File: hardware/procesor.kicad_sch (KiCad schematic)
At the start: 14 parts

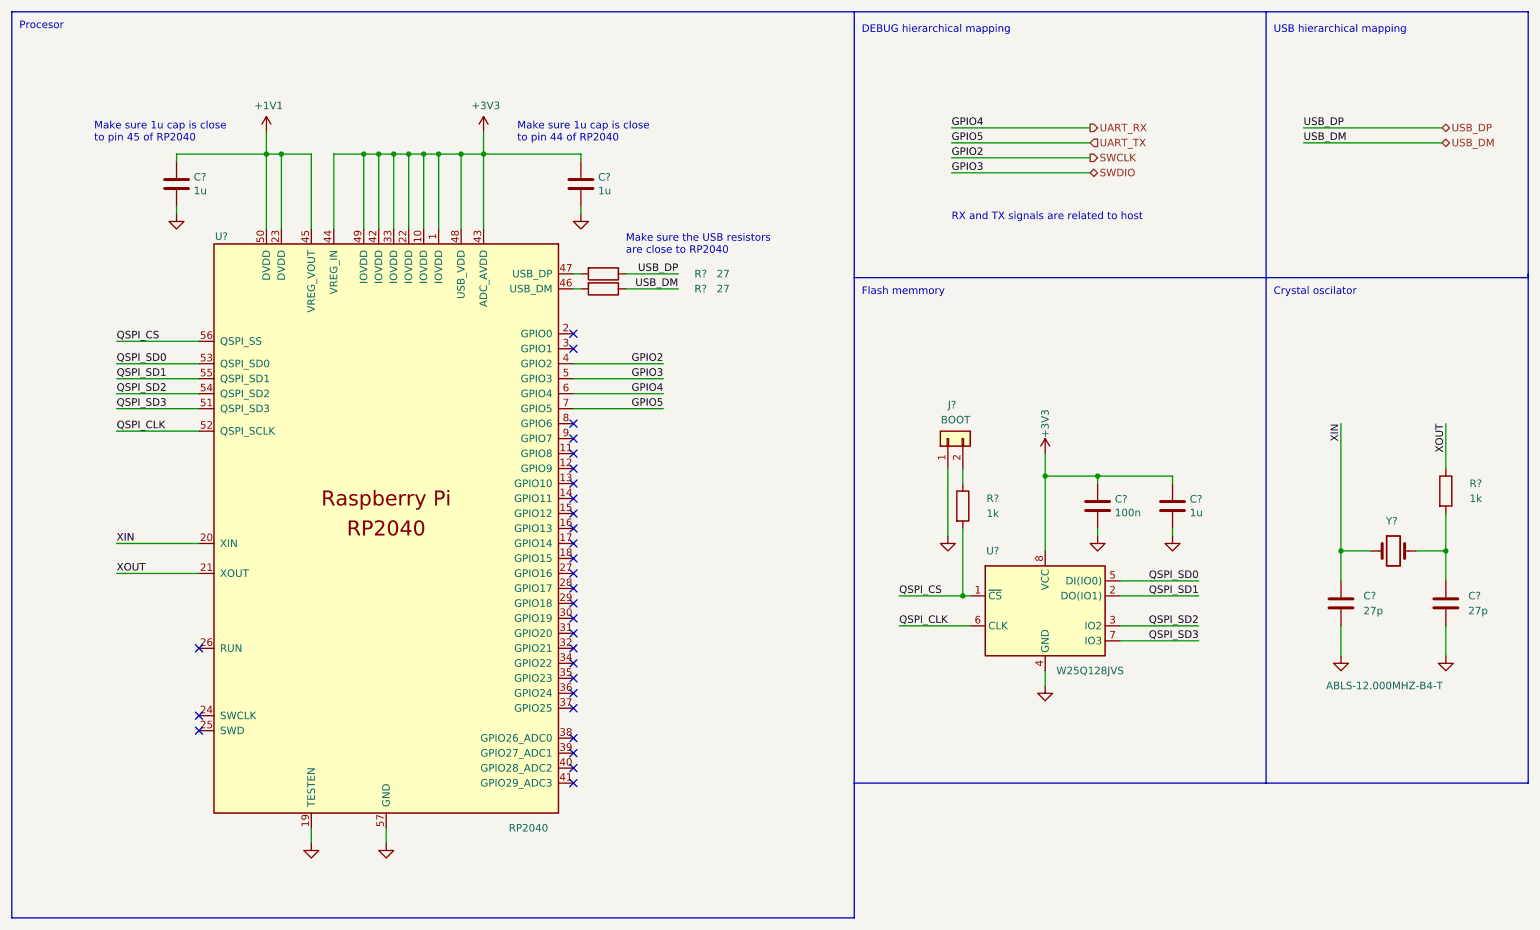
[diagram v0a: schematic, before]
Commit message: hw: Add annotations to all components
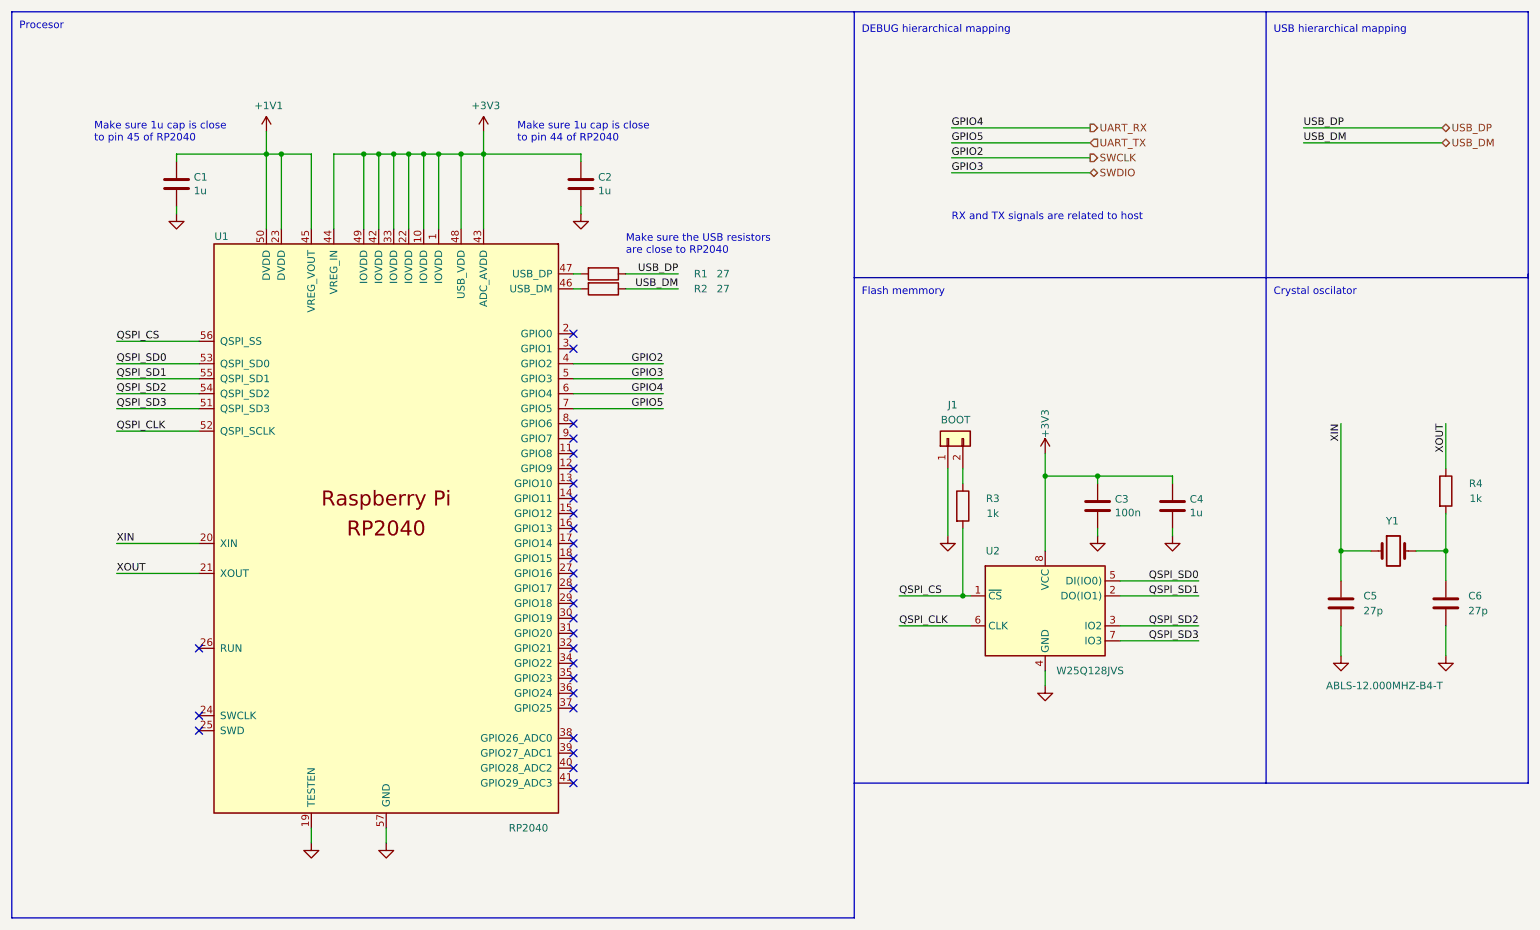
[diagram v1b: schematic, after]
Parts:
- gave numbers to parts that had none: 14
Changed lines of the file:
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@@
   (no_connect (at 114.935 158.115))
   (no_connect (at 114.935 160.655))
+  (no_connect (at 51.435 137.795))
   (no_connect (at 51.435 151.765))
   (no_connect (at 51.435 149.225))
-  (no_connect (at 51.435 137.795))
   (wire (pts (xy 99.695 50.165) (xy 99.695 53.975))
     (stroke (width 0) (type default) (color 0 0 0 0))
@@
   (symbol (lib_id "power:GND") (at 216.535 118.745 0) (unit 1)
     (in_bom yes) (on_board yes)
-    (property "Reference" "#PWR?" (id 0) (at 216.535 125.095 0)
+    (property "Reference" "#PWR011" (id 0) (at 216.535 125.095 0)
       (effects (font (size 1.27 1.27)) hide)
     )
@@
   (symbol (lib_id "Device:C") (at 116.205 59.055 0) (unit 1)
     (in_bom yes) (on_board yes)
-    (property "Reference" "C?" (id 0) (at 119.126 57.8866 0)
+    (property "Reference" "C2" (id 0) (at 119.126 57.8866 0)
       (effects (font (size 1.27 1.27)) (justify left))
     )
@@
   (symbol (lib_id "Device:C") (at 216.535 113.665 0) (unit 1)
     (in_bom yes) (on_board yes)
-    (property "Reference" "C?" (id 0) (at 219.456 112.4966 0)
+    (property "Reference" "C4" (id 0) (at 219.456 112.4966 0)
       (effects (font (size 1.27 1.27)) (justify left))
     )
@@
   (symbol (lib_id "power:GND") (at 83.185 170.815 0) (unit 1)
     (in_bom yes) (on_board yes)
-    (property "Reference" "#PWR?" (id 0) (at 83.185 177.165 0)
+    (property "Reference" "#PWR04" (id 0) (at 83.185 177.165 0)
       (effects (font (size 1.27 1.27)) hide)
     )
@@
   (symbol (lib_id "Device:R") (at 262.89 111.125 0) (unit 1)
     (in_bom yes) (on_board yes)
-    (property "Reference" "R?" (id 0) (at 267.97 109.855 0))
+    (property "Reference" "R4" (id 0) (at 267.97 109.855 0))
     (property "Value" "1k" (id 1) (at 267.97 112.395 0))
     (property "Footprint" "Capacitor_SMD:C_0603_1608Metric_Pad1.08x0.95mm_HandSolder" (id 2) (at 261.112 111.125 90)
@@
   (symbol (lib_id "Device:C") (at 47.625 59.055 0) (unit 1)
     (in_bom yes) (on_board yes)
-    (property "Reference" "C?" (id 0) (at 50.546 57.8866 0)
+    (property "Reference" "C1" (id 0) (at 50.546 57.8866 0)
       (effects (font (size 1.27 1.27)) (justify left))
     )
@@
   (symbol (lib_id "Memory_Flash:W25Q128JVS") (at 194.945 131.445 0) (unit 1)
     (in_bom yes) (on_board yes)
-    (property "Reference" "U?" (id 0) (at 186.055 121.285 0))
+    (property "Reference" "U2" (id 0) (at 186.055 121.285 0))
     (property "Value" "W25Q128JVS" (id 1) (at 202.565 141.605 0))
     (property "Footprint" "Package_SO:SOIC-8_5.23x5.23mm_P1.27mm" (id 2) (at 194.945 131.445 0)
@@
   (symbol (lib_id "power:GND") (at 47.625 64.135 0) (unit 1)
     (in_bom yes) (on_board yes)
-    (property "Reference" "#PWR?" (id 0) (at 47.625 70.485 0)
+    (property "Reference" "#PWR01" (id 0) (at 47.625 70.485 0)
       (effects (font (size 1.27 1.27)) hide)
     )
@@
   (symbol (lib_id "Device:C") (at 245.11 130.175 0) (unit 1)
     (in_bom yes) (on_board yes)
-    (property "Reference" "C?" (id 0) (at 248.92 128.905 0)
+    (property "Reference" "C5" (id 0) (at 248.92 128.905 0)
       (effects (font (size 1.27 1.27)) (justify left))
     )
@@
   (symbol (lib_id "Device:C") (at 203.835 113.665 0) (unit 1)
     (in_bom yes) (on_board yes)
-    (property "Reference" "C?" (id 0) (at 206.756 112.4966 0)
+    (property "Reference" "C3" (id 0) (at 206.756 112.4966 0)
       (effects (font (size 1.27 1.27)) (justify left))
     )
@@
   (symbol (lib_id "power:GND") (at 178.435 118.745 0) (unit 1)
     (in_bom yes) (on_board yes)
-    (property "Reference" "#PWR?" (id 0) (at 178.435 125.095 0)
+    (property "Reference" "#PWR07" (id 0) (at 178.435 125.095 0)
       (effects (font (size 1.27 1.27)) hide)
     )
@@
   (symbol (lib_id "Device:Crystal") (at 254 121.285 0) (unit 1)
     (in_bom yes) (on_board yes)
-    (property "Reference" "Y?" (id 0) (at 252.73 116.205 0)
+    (property "Reference" "Y1" (id 0) (at 252.73 116.205 0)
       (effects (font (size 1.27 1.27)) (justify left))
     )
@@
   (symbol (lib_id "power:+1V1") (at 62.865 50.165 0) (unit 1)
     (in_bom yes) (on_board yes)
-    (property "Reference" "#PWR?" (id 0) (at 62.865 53.975 0)
+    (property "Reference" "#PWR02" (id 0) (at 62.865 53.975 0)
       (effects (font (size 1.27 1.27)) hide)
     )
@@
   (symbol (lib_id "power:+3V3") (at 99.695 50.165 0) (unit 1)
     (in_bom yes) (on_board yes)
-    (property "Reference" "#PWR?" (id 0) (at 99.695 53.975 0)
+    (property "Reference" "#PWR05" (id 0) (at 99.695 53.975 0)
       (effects (font (size 1.27 1.27)) hide)
     )
@@
   (symbol (lib_id "Connector_Generic:Conn_01x02") (at 178.435 102.235 90) (unit 1)
     (in_bom yes) (on_board yes)
-    (property "Reference" "J?" (id 0) (at 178.435 96.52 90)
+    (property "Reference" "J1" (id 0) (at 178.435 96.52 90)
       (effects (font (size 1.27 1.27)) (justify right))
     )
@@
   (symbol (lib_id "power:GND") (at 194.945 144.145 0) (unit 1)
     (in_bom yes) (on_board yes)
-    (property "Reference" "#PWR?" (id 0) (at 194.945 150.495 0)
+    (property "Reference" "#PWR09" (id 0) (at 194.945 150.495 0)
       (effects (font (size 1.27 1.27)) hide)
     )
@@
   (symbol (lib_id "power:GND") (at 262.89 139.065 0) (unit 1)
     (in_bom yes) (on_board yes)
-    (property "Reference" "#PWR?" (id 0) (at 262.89 145.415 0)
+    (property "Reference" "#PWR013" (id 0) (at 262.89 145.415 0)
       (effects (font (size 1.27 1.27)) hide)
     )
@@
   (symbol (lib_id "Device:C") (at 262.89 130.175 0) (unit 1)
     (in_bom yes) (on_board yes)
-    (property "Reference" "C?" (id 0) (at 266.7 128.905 0)
+    (property "Reference" "C6" (id 0) (at 266.7 128.905 0)
       (effects (font (size 1.27 1.27)) (justify left))
     )
@@
   (symbol (lib_id "MCU_RaspberryPi_RP2040:RP2040") (at 83.185 117.475 0) (unit 1)
     (in_bom yes) (on_board yes)
-    (property "Reference" "U?" (id 0) (at 55.245 67.945 0))
+    (property "Reference" "U1" (id 0) (at 55.245 67.945 0))
     (property "Value" "RP2040" (id 1) (at 107.315 168.275 0))
     (property "Footprint" "RP2040:RP2040-QFN-56" (id 2) (at 64.135 117.475 0)
@@
   (symbol (lib_id "Device:R") (at 180.975 113.665 0) (unit 1)
     (in_bom yes) (on_board yes)
-    (property "Reference" "R?" (id 0) (at 186.055 112.395 0))
+    (property "Reference" "R3" (id 0) (at 186.055 112.395 0))
     (property "Value" "1k" (id 1) (at 186.055 114.935 0))
     (property "Footprint" "Capacitor_SMD:C_0603_1608Metric_Pad1.08x0.95mm_HandSolder" (id 2) (at 179.197 113.665 90)
@@
   (symbol (lib_id "power:+3V3") (at 194.945 104.775 0) (unit 1)
     (in_bom yes) (on_board yes)
-    (property "Reference" "#PWR?" (id 0) (at 194.945 108.585 0)
+    (property "Reference" "#PWR08" (id 0) (at 194.945 108.585 0)
       (effects (font (size 1.27 1.27)) hide)
     )
@@
   (symbol (lib_id "power:GND") (at 203.835 118.745 0) (unit 1)
     (in_bom yes) (on_board yes)
-    (property "Reference" "#PWR?" (id 0) (at 203.835 125.095 0)
+    (property "Reference" "#PWR010" (id 0) (at 203.835 125.095 0)
       (effects (font (size 1.27 1.27)) hide)
     )
@@
   (symbol (lib_id "Device:R") (at 120.015 74.295 270) (unit 1)
     (in_bom yes) (on_board yes)
-    (property "Reference" "R?" (id 0) (at 136.525 74.295 90))
+    (property "Reference" "R1" (id 0) (at 136.525 74.295 90))
     (property "Value" "27" (id 1) (at 140.335 74.295 90))
     (property "Footprint" "Capacitor_SMD:C_0603_1608Metric_Pad1.08x0.95mm_HandSolder" (id 2) (at 120.015 72.517 90)
@@
   (symbol (lib_id "Device:R") (at 120.015 76.835 270) (unit 1)
     (in_bom yes) (on_board yes)
-    (property "Reference" "R?" (id 0) (at 136.525 76.835 90))
+    (property "Reference" "R2" (id 0) (at 136.525 76.835 90))
     (property "Value" "27" (id 1) (at 140.335 76.835 90))
     (property "Footprint" "Capacitor_SMD:C_0603_1608Metric_Pad1.08x0.95mm_HandSolder" (id 2) (at 120.015 75.057 90)
@@
   (symbol (lib_id "power:GND") (at 70.485 170.815 0) (unit 1)
     (in_bom yes) (on_board yes)
-    (property "Reference" "#PWR?" (id 0) (at 70.485 177.165 0)
+    (property "Reference" "#PWR03" (id 0) (at 70.485 177.165 0)
       (effects (font (size 1.27 1.27)) hide)
     )
@@
   (symbol (lib_id "power:GND") (at 116.205 64.135 0) (unit 1)
     (in_bom yes) (on_board yes)
-    (property "Reference" "#PWR?" (id 0) (at 116.205 70.485 0)
+    (property "Reference" "#PWR06" (id 0) (at 116.205 70.485 0)
       (effects (font (size 1.27 1.27)) hide)
     )
@@
   (symbol (lib_id "power:GND") (at 245.11 139.065 0) (unit 1)
     (in_bom yes) (on_board yes)
-    (property "Reference" "#PWR?" (id 0) (at 245.11 145.415 0)
-      (effects (font (size 1.27 1.27)) hide)
-    )
+    (property "Reference" "#PWR012" (id 0) (at 245.11 145.415 0)
+      (effects (font (size 1.27 1.27)) hide)
+    )
